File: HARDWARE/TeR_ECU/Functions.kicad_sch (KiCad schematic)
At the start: 7 parts, among them Q1 ZXMN3F30FH, Q2 ZXMN3F30FH

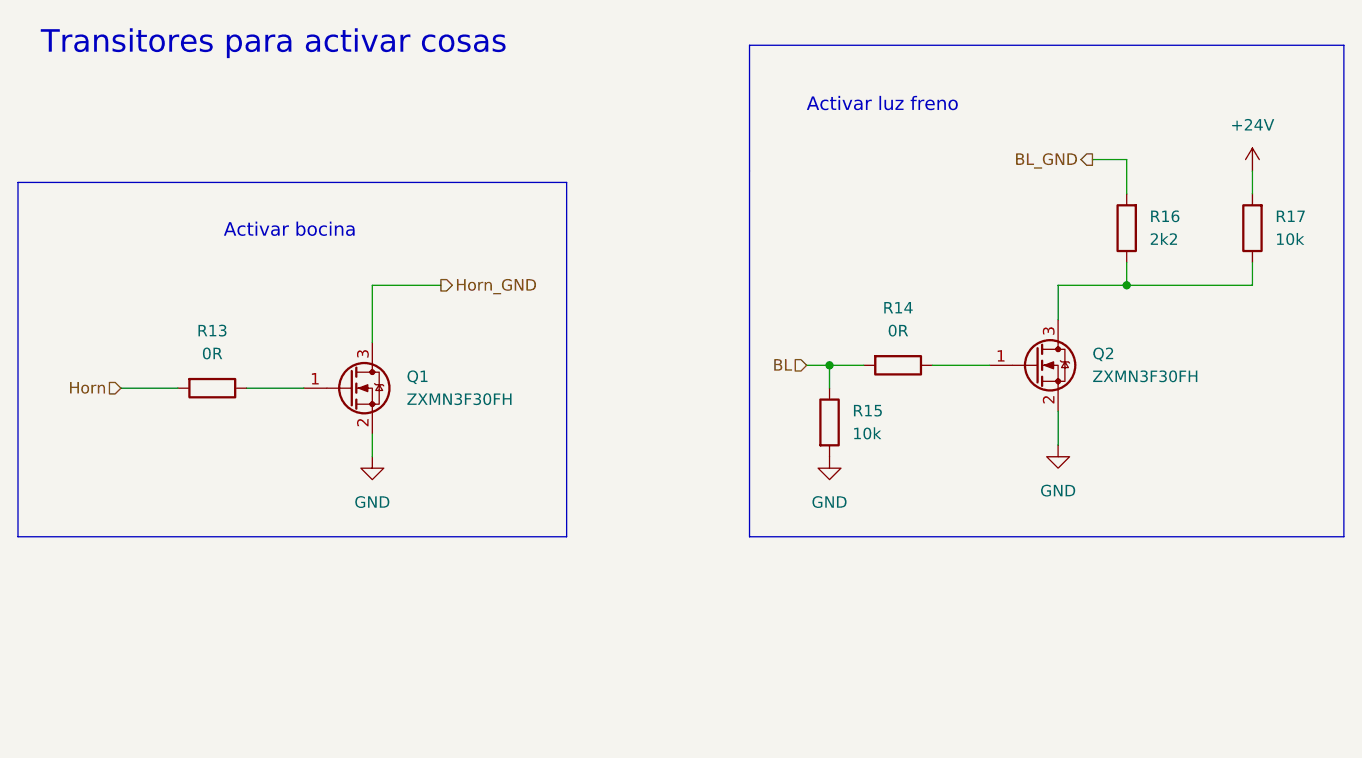
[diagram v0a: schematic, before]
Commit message: Rethought layout and footprints and fixed fuse normative problem
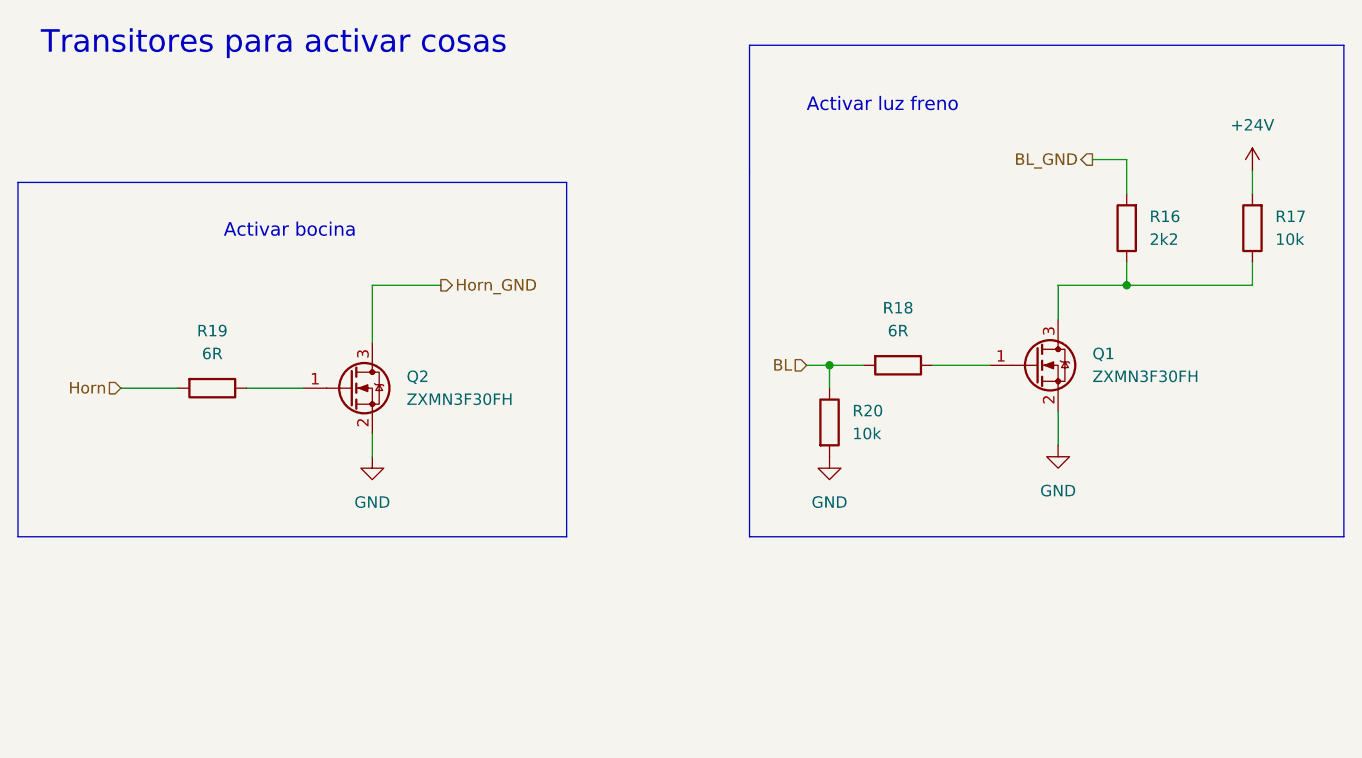
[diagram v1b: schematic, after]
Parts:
- R18: renamed from R14; value 0R -> 6R
- R19: renamed from R13; value 0R -> 6R
- renumbered Q2 to Q1, Q1 to Q2, R15 to R20
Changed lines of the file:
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@@
   (symbol (lib_id "Transistor_FET:ZXMN3F30FH") (at 99.06 72.39 0) (unit 1)
     (in_bom yes) (on_board yes) (dnp no) (fields_autoplaced)
-    (property "Reference" "Q1" (at 105.41 71.12 0)
+    (property "Reference" "Q2" (at 105.41 71.12 0)
       (effects (font (size 1.27 1.27)) (justify left))
     )
@@
       (project "TeR_ECU"
         (path "/84413845-c4f3-4743-bcd2-a67649c90902/3120aa2d-43f7-45e0-8e9f-779f72cfb5e6"
-          (reference "Q1") (unit 1)
+          (reference "Q2") (unit 1)
         )
       )
@@
   (symbol (lib_id "power:GND") (at 152.4 80.01 0) (unit 1)
     (in_bom yes) (on_board yes) (dnp no) (fields_autoplaced)
-    (property "Reference" "#PWR049" (at 152.4 86.36 0)
+    (property "Reference" "#PWR058" (at 152.4 86.36 0)
       (effects (font (size 1.27 1.27)) hide)
     )
@@
       (project "TeR_ECU"
         (path "/84413845-c4f3-4743-bcd2-a67649c90902/3120aa2d-43f7-45e0-8e9f-779f72cfb5e6"
-          (reference "#PWR049") (unit 1)
+          (reference "#PWR058") (unit 1)
         )
       )
@@
   (symbol (lib_id "power:GND") (at 101.6 80.01 0) (unit 1)
     (in_bom yes) (on_board yes) (dnp no) (fields_autoplaced)
-    (property "Reference" "#PWR047" (at 101.6 86.36 0)
+    (property "Reference" "#PWR057" (at 101.6 86.36 0)
       (effects (font (size 1.27 1.27)) hide)
     )
@@
       (project "TeR_ECU"
         (path "/84413845-c4f3-4743-bcd2-a67649c90902/3120aa2d-43f7-45e0-8e9f-779f72cfb5e6"
-          (reference "#PWR047") (unit 1)
+          (reference "#PWR057") (unit 1)
         )
       )
@@
   (symbol (lib_id "Device:R") (at 83.82 72.39 270) (unit 1)
     (in_bom yes) (on_board yes) (dnp no) (fields_autoplaced)
-    (property "Reference" "R13" (at 83.82 66.04 90)
-      (effects (font (size 1.27 1.27)))
-    )
-    (property "Value" "0R" (at 83.82 68.58 90)
+    (property "Reference" "R19" (at 83.82 66.04 90)
+      (effects (font (size 1.27 1.27)))
+    )
+    (property "Value" "6R" (at 83.82 68.58 90)
       (effects (font (size 1.27 1.27)))
     )
@@
       (project "TeR_ECU"
         (path "/84413845-c4f3-4743-bcd2-a67649c90902/3120aa2d-43f7-45e0-8e9f-779f72cfb5e6"
-          (reference "R13") (unit 1)
+          (reference "R19") (unit 1)
         )
       )
@@
   (symbol (lib_id "power:GND") (at 177.8 78.74 0) (unit 1)
     (in_bom yes) (on_board yes) (dnp no) (fields_autoplaced)
-    (property "Reference" "#PWR048" (at 177.8 85.09 0)
+    (property "Reference" "#PWR056" (at 177.8 85.09 0)
       (effects (font (size 1.27 1.27)) hide)
     )
@@
       (project "TeR_ECU"
         (path "/84413845-c4f3-4743-bcd2-a67649c90902/3120aa2d-43f7-45e0-8e9f-779f72cfb5e6"
-          (reference "#PWR048") (unit 1)
+          (reference "#PWR056") (unit 1)
         )
       )
@@
   (symbol (lib_id "power:+24V") (at 199.39 48.26 0) (unit 1)
     (in_bom yes) (on_board yes) (dnp no) (fields_autoplaced)
-    (property "Reference" "#PWR050" (at 199.39 52.07 0)
+    (property "Reference" "#PWR055" (at 199.39 52.07 0)
       (effects (font (size 1.27 1.27)) hide)
     )
@@
       (project "TeR_ECU"
         (path "/84413845-c4f3-4743-bcd2-a67649c90902/3120aa2d-43f7-45e0-8e9f-779f72cfb5e6"
-          (reference "#PWR050") (unit 1)
+          (reference "#PWR055") (unit 1)
         )
       )
@@
   (symbol (lib_id "Device:R") (at 152.4 76.2 0) (unit 1)
     (in_bom yes) (on_board yes) (dnp no) (fields_autoplaced)
-    (property "Reference" "R15" (at 154.94 74.93 0)
+    (property "Reference" "R20" (at 154.94 74.93 0)
       (effects (font (size 1.27 1.27)) (justify left))
     )
@@
       (project "TeR_ECU"
         (path "/84413845-c4f3-4743-bcd2-a67649c90902/3120aa2d-43f7-45e0-8e9f-779f72cfb5e6"
-          (reference "R15") (unit 1)
+          (reference "R20") (unit 1)
         )
       )
@@
   (symbol (lib_id "Transistor_FET:ZXMN3F30FH") (at 175.26 69.85 0) (unit 1)
     (in_bom yes) (on_board yes) (dnp no) (fields_autoplaced)
-    (property "Reference" "Q2" (at 181.61 68.58 0)
+    (property "Reference" "Q1" (at 181.61 68.58 0)
       (effects (font (size 1.27 1.27)) (justify left))
     )
@@
       (project "TeR_ECU"
         (path "/84413845-c4f3-4743-bcd2-a67649c90902/3120aa2d-43f7-45e0-8e9f-779f72cfb5e6"
-          (reference "Q2") (unit 1)
+          (reference "Q1") (unit 1)
         )
       )
@@
   (symbol (lib_id "Device:R") (at 160.02 69.85 270) (unit 1)
     (in_bom yes) (on_board yes) (dnp no) (fields_autoplaced)
-    (property "Reference" "R14" (at 160.02 63.5 90)
-      (effects (font (size 1.27 1.27)))
-    )
-    (property "Value" "0R" (at 160.02 66.04 90)
+    (property "Reference" "R18" (at 160.02 63.5 90)
+      (effects (font (size 1.27 1.27)))
+    )
+    (property "Value" "6R" (at 160.02 66.04 90)
       (effects (font (size 1.27 1.27)))
     )
@@
       (project "TeR_ECU"
         (path "/84413845-c4f3-4743-bcd2-a67649c90902/3120aa2d-43f7-45e0-8e9f-779f72cfb5e6"
-          (reference "R14") (unit 1)
-        )
-      )
+          (reference "R18") (unit 1)
+        )
+      )

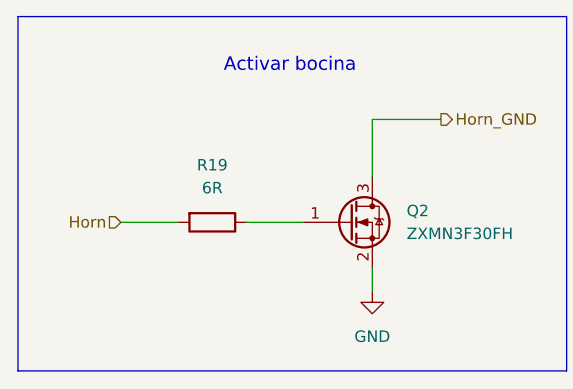
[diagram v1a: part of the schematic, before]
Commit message: Rethought layout and added pulldown to Horn mosfet
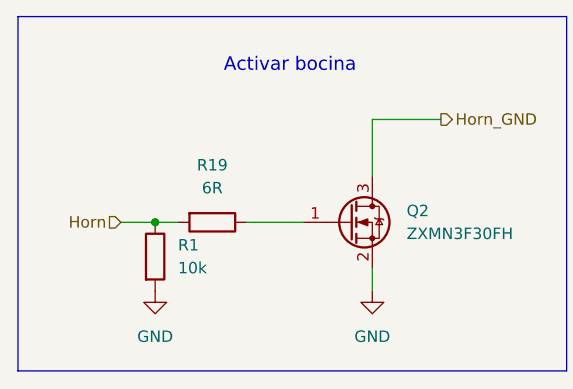
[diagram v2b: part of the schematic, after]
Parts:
- added R1: 10k, Resistor_SMD:R_0805_2012Metric, symbol Device:R
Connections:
- net GND: now also R1.2
- net Horn: now also R1.1
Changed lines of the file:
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@@
   (junction (at 185.42 60.96) (diameter 0) (color 0 0 0 0)
   )
+  (junction (at 77.47 72.39) (diameter 0) (color 0 0 0 0)
+  )
   (wire (pts (xy 177.8 60.96) (xy 185.42 60.96))
     (stroke (width 0) (type default))
@@
     (stroke (width 0) (type default))
   )
-  (wire (pts (xy 73.66 72.39) (xy 80.01 72.39))
+  (wire (pts (xy 73.66 72.39) (xy 77.47 72.39))
     (stroke (width 0) (type default))
   )
@@
   )
   (wire (pts (xy 101.6 67.31) (xy 101.6 60.96))
+    (stroke (width 0) (type default))
+  )
+  (wire (pts (xy 77.47 72.39) (xy 80.01 72.39))
     (stroke (width 0) (type default))
   )
@@
     )
   )
+  (symbol (lib_id "Device:R") (at 77.47 76.2 0) (unit 1)
+    (in_bom yes) (on_board yes) (dnp no) (fields_autoplaced)
+    (property "Reference" "R1" (at 80.01 74.93 0)
+      (effects (font (size 1.27 1.27)) (justify left))
+    )
+    (property "Value" "10k" (at 80.01 77.47 0)
+      (effects (font (size 1.27 1.27)) (justify left))
+    )
+    (property "Footprint" "Resistor_SMD:R_0805_2012Metric" (at 75.692 76.2 90)
+      (effects (font (size 1.27 1.27)) hide)
+    )
+    (property "Datasheet" "~" (at 77.47 76.2 0)
+      (effects (font (size 1.27 1.27)) hide)
+    )
+    (pin "1")
+    (pin "2")
+    (instances
+      (project "TeR_ECU"
+        (path "/84413845-c4f3-4743-bcd2-a67649c90902/3120aa2d-43f7-45e0-8e9f-779f72cfb5e6"
+          (reference "R1") (unit 1)
+        )
+      )
+    )
+  )
   (symbol (lib_id "power:GND") (at 152.4 80.01 0) (unit 1)
     (in_bom yes) (on_board yes) (dnp no) (fields_autoplaced)
@@
         )
       )
+    )
+  )
+  (symbol (lib_id "power:GND") (at 77.47 80.01 0) (unit 1)
+    (in_bom yes) (on_board yes) (dnp no) (fields_autoplaced)
+    (property "Reference" "#PWR01" (at 77.47 86.36 0)
+      (effects (font (size 1.27 1.27)) hide)
+    )
+    (property "Value" "GND" (at 77.47 85.09 0)
+      (effects (font (size 1.27 1.27)))
+    )
+    (property "Footprint" "" (at 77.47 80.01 0)
+      (effects (font (size 1.27 1.27)) hide)
+    )
+    (property "Datasheet" "" (at 77.47 80.01 0)
+      (effects (font (size 1.27 1.27)) hide)
+    )
+    (pin "1")
+    (instances
+      (project "TeR_ECU"
+        (path "/84413845-c4f3-4743-bcd2-a67649c90902/3120aa2d-43f7-45e0-8e9f-779f72cfb5e6"
+          (reference "#PWR01") (unit 1)
+        )
+      )

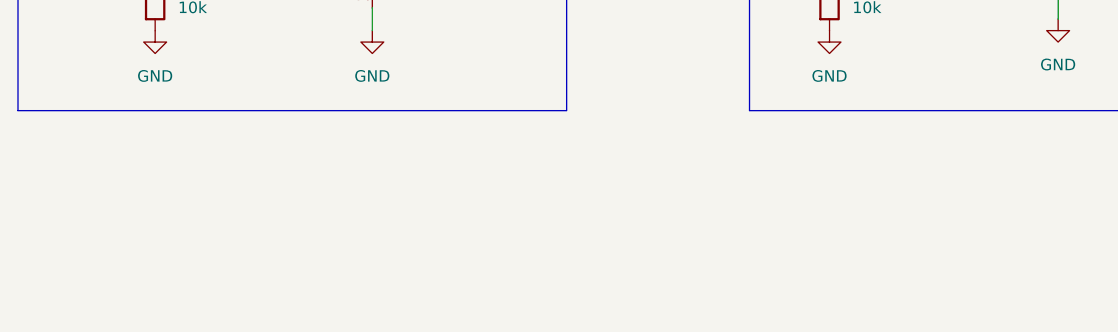
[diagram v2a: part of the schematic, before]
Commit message: Layout V2, added 7-segment display, optimal placement of pins + rework of the boot headers(just one needed)
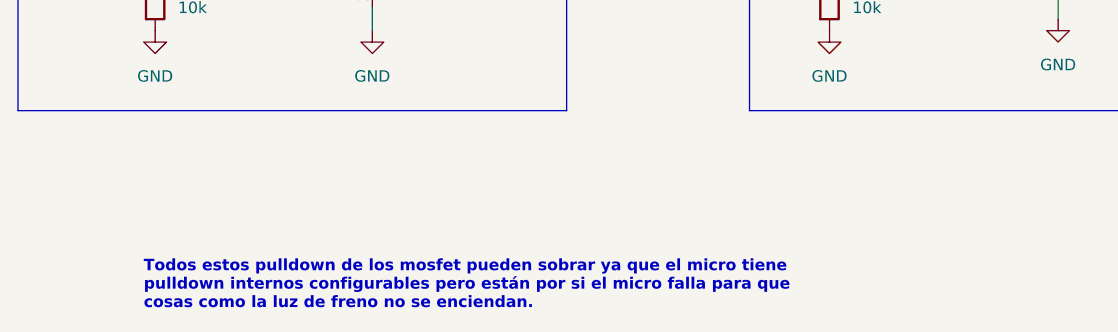
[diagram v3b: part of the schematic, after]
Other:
- note added: "Todos estos pulldown de los mosfet pueden sobrar ya que el micro tiene pulldown internos configurables pero están por si el micro falla para que cosas como la luz de freno no se enciendan."
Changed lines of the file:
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@@
     (stroke (width 0) (type default))
+  )
+  (text "Todos estos pulldown de los mosfet pueden sobrar ya que el micro tiene\npulldown internos configurables pero están por si el micro falla para que \ncosas como la luz de freno no se enciendan."
+    (at 76.2 111.125 0)
+    (effects (font (size 1.27 1.27) bold) (justify left bottom))
   )
   (text "Transitores para activar cosas\n" (at 64.77 35.56 0)
